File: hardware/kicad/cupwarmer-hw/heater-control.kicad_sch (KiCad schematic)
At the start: 10 parts, among them Q1 AO3400 SOT-23

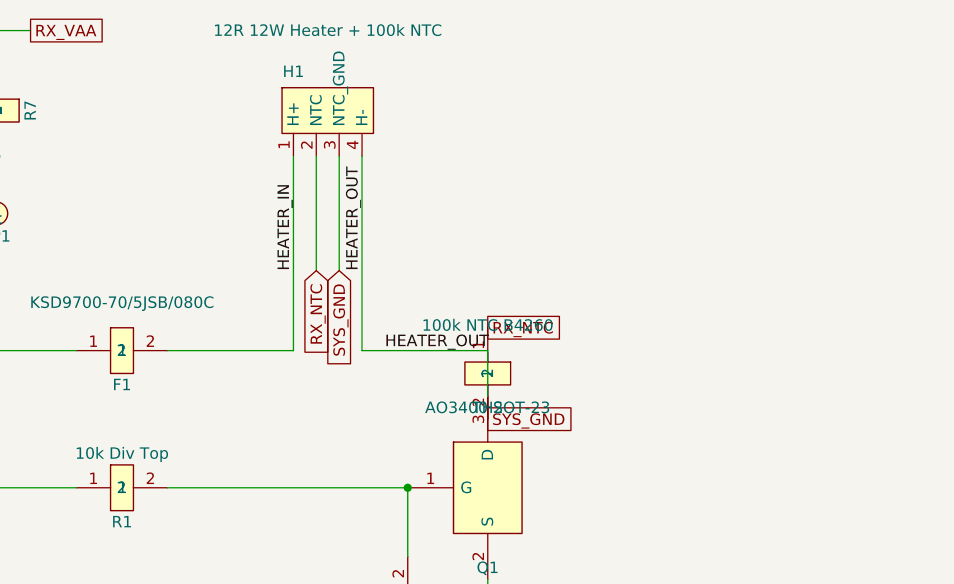
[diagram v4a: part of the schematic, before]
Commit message: Add R_HTR off-board to model heater coil; relabel H1
Pair TH2 with R_HTR (12 ohm, 12 W coil) so the heater assembly's
internals (heater + NTC) are explicit on the schematic but excluded
from the board (on_board=no, empty Footprint). H1's Value drops
the redundant element description and now reads "4-pin heater
harness connector" — H1 is just the connector boundary; the actual
parts live in R_HTR and TH2.

Co-Authored-By: Claude Opus 4.7 (1M context) <noreply@anthropic.com>
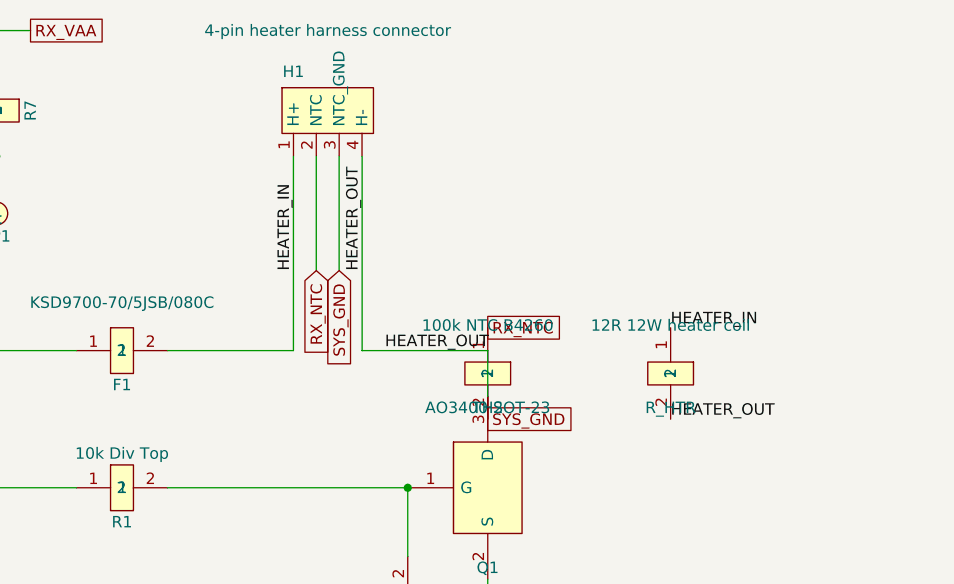
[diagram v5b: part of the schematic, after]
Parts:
- added R_HTR: 12R 12W heater coil, symbol cupwarmer:PASSIVE_2
- H1: value 12R 12W Heater + 100k NTC -> 4-pin heater harness connector
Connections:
- net HEATER_IN: now also R_HTR.1
- net HEATER_OUT: now also R_HTR.2
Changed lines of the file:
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@@
+	)
+	(label "HEATER_OUT"
+		(at 116.84 66.04 0)
+		(effects
+			(font
+				(size 1.27 1.27)
+			)
+			(justify left bottom)
+		)
+	)
+	(label "HEATER_IN"
+		(at 116.84 55.88 0)
+		(effects
+			(font
+				(size 1.27 1.27)
+			)
+			(justify left bottom)
+		)
 	)
 	(label "HEATER_OUT"
@@
 	(symbol
 		(lib_id "cupwarmer:PASSIVE_2")
+		(at 116.84 60.96 270)
+		(unit 1)
+		(body_style 1)
+		(exclude_from_sim no)
+		(in_bom yes)
+		(on_board no)
+		(in_pos_files yes)
+		(dnp no)
+		(property "Reference" "R_HTR"
+			(at 116.84 64.77 270)
+			(show_name no)
+			(do_not_autoplace no)
+			(effects
+				(font
+					(size 1.27 1.27)
+				)
+			)
+		)
+		(property "Value" "12R 12W heater coil"
+			(at 116.84 55.626 270)
+			(show_name no)
+			(do_not_autoplace no)
+			(effects
+				(font
+					(size 1.27 1.27)
+				)
+			)
+		)
+		(property "Footprint" ""
+			(at 116.84 60.96 270)
+			(hide yes)
+			(show_name no)
+			(do_not_autoplace no)
+			(effects
+				(font
+					(size 1.27 1.27)
+				)
+			)
+		)
+		(property "Datasheet" "~"
+			(at 116.84 60.96 270)
+			(hide yes)
+			(show_name no)
+			(do_not_autoplace no)
+			(effects
+				(font
+					(size 1.27 1.27)
+				)
+			)
+		)
+		(property "Description" "Silicone heater element inside H1 harness; 12 ohm, 12 W nominal, off-board"
+			(at 116.84 60.96 270)
+			(hide yes)
+			(show_name no)
+			(do_not_autoplace no)
+			(effects
+				(font
+					(size 1.27 1.27)
+				)
+			)
+		)
+		(property "Manufacturer" ""
+			(at 0 0 0)
+			(hide yes)
+			(show_name no)
+			(do_not_autoplace no)
+			(effects
+				(font
+					(size 1.27 1.27)
+				)
+			)
+		)
+		(property "LCSC" ""
+			(at 0 0 0)
+			(hide yes)
+			(show_name no)
+			(do_not_autoplace no)
+			(effects
+				(font
+					(size 1.27 1.27)
+				)
+			)
+		)
+		(property "MPN" ""
+			(at 0 0 0)
+			(hide yes)
+			(show_name no)
+			(do_not_autoplace no)
+			(effects
+				(font
+					(size 1.27 1.27)
+				)
+			)
+		)
+		(pin "1"
+		)
+		(pin "2"
+		)
+		(instances
+			(project "cupwarmer-hw"
+				(path "/f3c63676-f392-4700-9f58-a6787e1eb284/22222222-2222-2222-2222-222222222222"
+					(reference "R_HTR")
+					(unit 1)
+				)
+			)
+		)
+	)
+	(symbol
+		(lib_id "cupwarmer:PASSIVE_2")
 		(at 96.52 60.96 270)
 		(unit 1)
@@
 			)
 		)
-		(property "Value" "12R 12W Heater + 100k NTC"
+		(property "Value" "4-pin heater harness connector"
 			(at 78.74 22.86 0)
 			(show_name no)

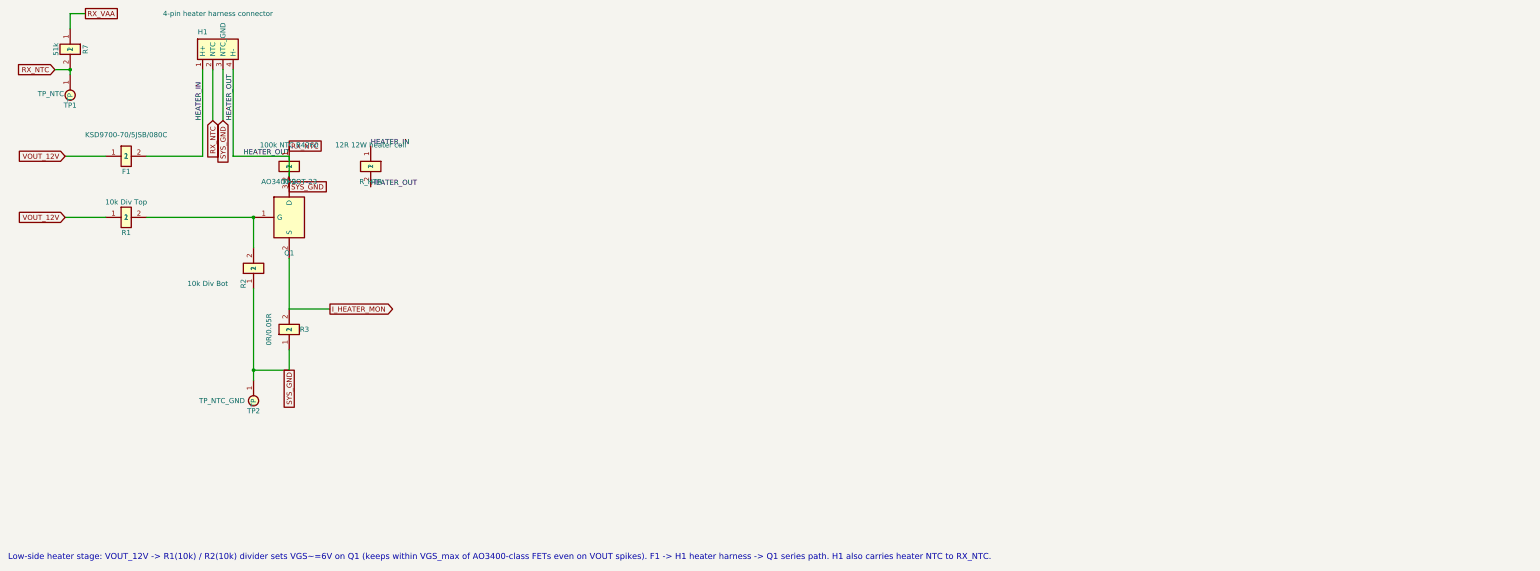
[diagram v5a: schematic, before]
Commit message: Mark H2 off-board; relabel H1/H2 as PCB-side / heater-side
Add H2 as the heater-side 4-pin connector, paired with H1 on the PCB
side. H2/F1/TH2/R_HTR remain visible on the schematic for
documentation of the heater assembly, but are excluded from the PCB
netlist via on_board=no.

Co-Authored-By: Claude Opus 4.7 (1M context) <noreply@anthropic.com>
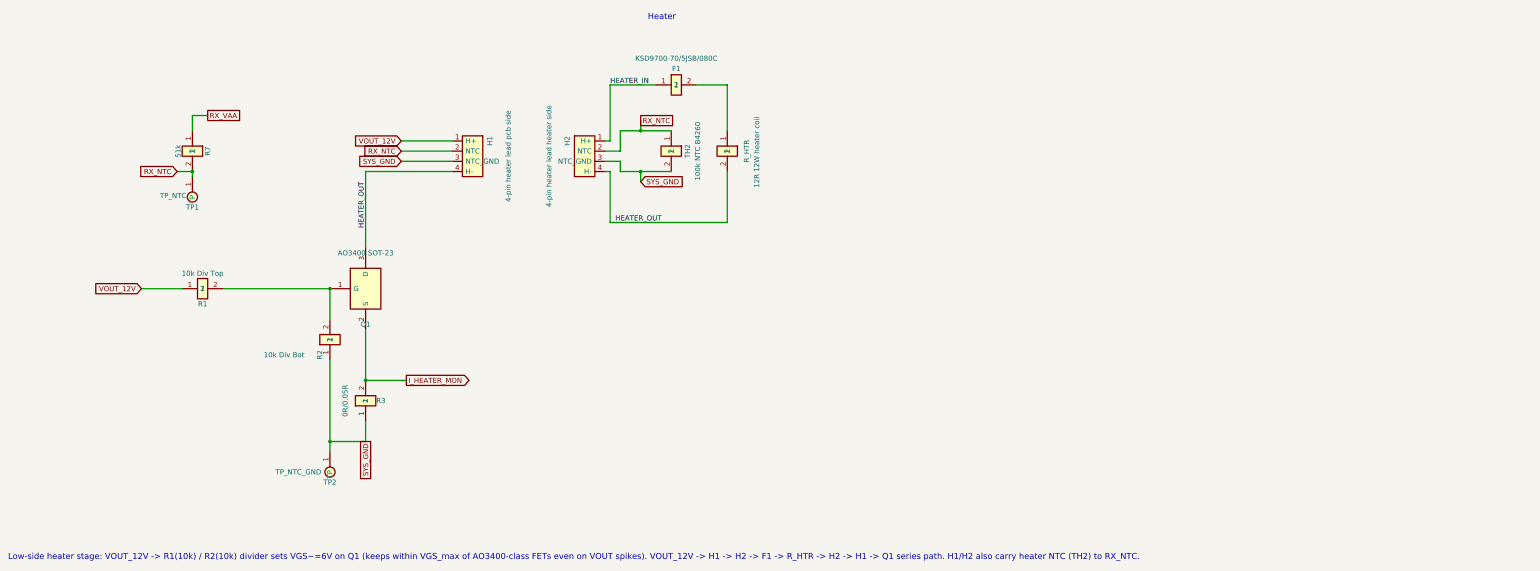
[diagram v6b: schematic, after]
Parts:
- added H2: 4-pin heater lead heater side, cupwarmer:SolderWire-HeaterHarness_1x04_P5.0mm_D1.4mm, symbol cupwarmer:HEATER_HARNESS_4
- H1: value 4-pin heater harness connector -> 4-pin heater lead pcb side
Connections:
- net HEATER_IN: now also F1.1, H2.1 (H+); no longer F1.2, H1.1 (H+), R_HTR.1
- net HEATER_OUT: now also H2.4 (H-)
- net RX_NTC: now also H2.2 (NTC)
- net SYS_GND: now also H2.3 (NTC_GND)
- net VOUT_12V: now also H1.1 (H+); no longer F1.1
- new net: F1.2, R_HTR.1
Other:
- note added: "Heater"
- note added: "Low-side heater stage: VOUT_12V -> R1(10k) / R2(10k) divider sets VGS~=6V on Q1 (keeps within VGS_max of AO3400-class FETs even on VOUT spikes). VOUT_12V -> H1 -> H2 -> F1 -> R_HTR -> H2 -> H1 -> Q1 series path. H1/H2 also carry heater NTC (TH2) to RX_NTC."
- note removed: "Low-side heater stage: VOUT_12V -> R1(10k) / R2(10k) divider sets VGS~=6V on Q1 (keeps within VGS_max of AO3400-class FETs even on VOUT spikes). F1 -> H1 heater harness -> Q1 series path. H1 also carries heater NTC to RX_NTC."
- moved on the sheet: F1, H1, Q1, R1, R2, R3, R7, R_HTR, TH2, TP1, TP2

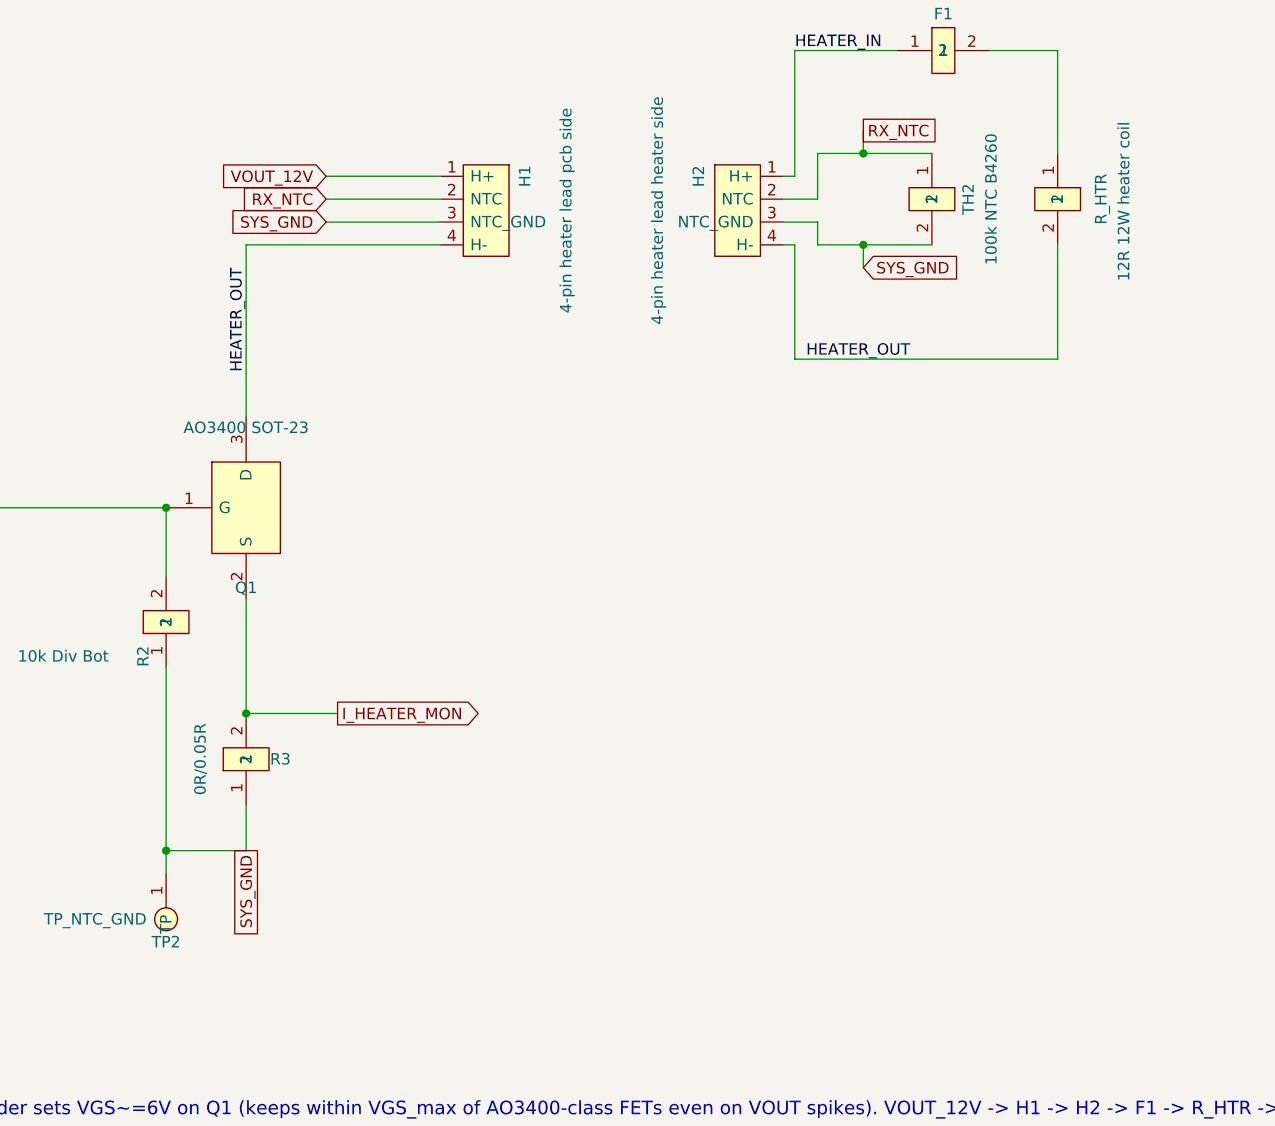
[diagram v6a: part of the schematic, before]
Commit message: Replace J3 bring-up header with TP3 test pad on I_HEATER_MON
Drop the dual-purpose 2-pin J3 (RX_INTB + I_HEATER_MON bring-up) and
expose only I_HEATER_MON via a single-pin TP3 test pad matching
TP1/TP2 (TESTPAD_1 symbol, 1x01 pin header footprint). RX_INTB stays
internal to the U1.H4 ↔ R12.1 path with its label moved onto that
net.

Co-Authored-By: Claude Opus 4.7 (1M context) <noreply@anthropic.com>
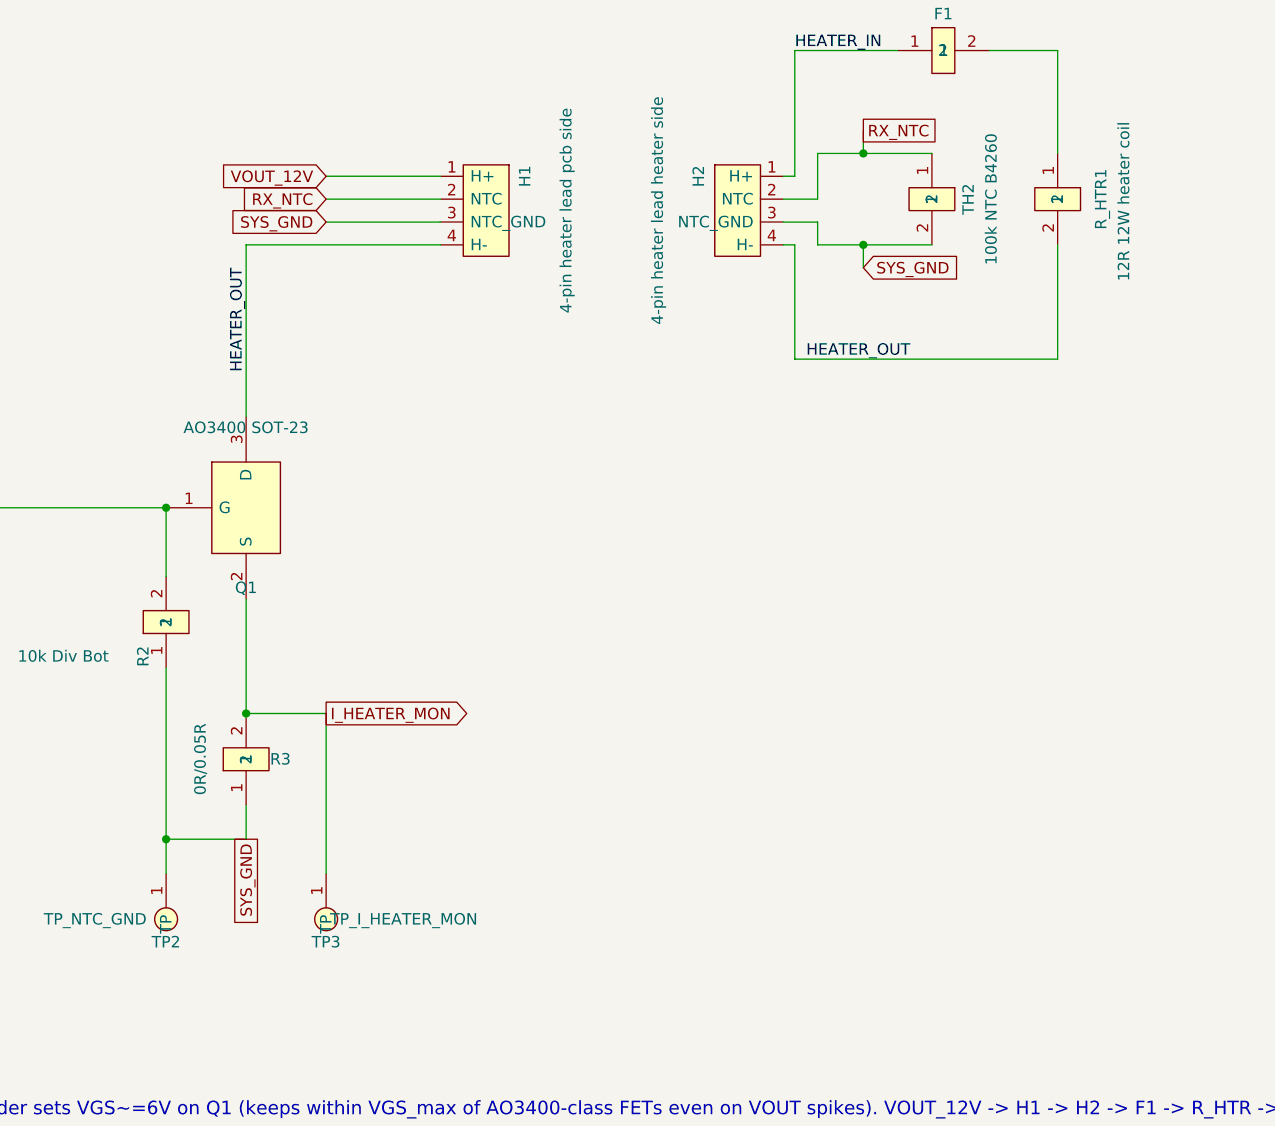
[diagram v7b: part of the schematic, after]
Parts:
- added TP3: TP_I_HEATER_MON, Connector_PinHeader_2.54mm:PinHeader_1x01_P2.54mm_Vertical, symbol cupwarmer:TESTPAD_1
- TP1, TP2: footprint cupwarmer:TestPoint_Pad_D1.0mm_NoSilk -> Connector_PinHeader_2.54mm:PinHeader_1x01_P2.54mm_Vertical
- renumbered R_HTR to R_HTR1
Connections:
- net I_HEATER_MON: now also TP3.1 (TP)
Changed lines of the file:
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@@
+	)
+	(junction
+		(at 106.68 128.27)
+		(diameter 0)
+		(color 0 0 0 0)
 	)
 	(junction
@@
 	)
 	(junction
-		(at 115.57 114.3)
+		(at 72.39 62.23)
 		(diameter 0)
 		(color 0 0 0 0)
 	)
 	(junction
-		(at 106.68 129.54)
-		(diameter 0)
-		(color 0 0 0 0)
-	)
-	(junction
-		(at 72.39 62.23)
+		(at 115.57 114.3)
 		(diameter 0)
 		(color 0 0 0 0)
@@
 	(wire
 		(pts
-			(xy 106.68 132.08) (xy 106.68 129.54)
-		)
-		(stroke
-			(width 0)
-			(type default)
-		)
-	)
-	(wire
-		(pts
 			(xy 115.57 101.6) (xy 115.57 114.3)
 		)
@@
 	(wire
 		(pts
-			(xy 115.57 124.46) (xy 115.57 129.54)
+			(xy 115.57 124.46) (xy 115.57 128.27)
 		)
 		(stroke
@@
 	(wire
 		(pts
-			(xy 115.57 114.3) (xy 125.73 114.3)
+			(xy 115.57 114.3) (xy 124.46 114.3)
 		)
 		(stroke
@@
 	(wire
 		(pts
-			(xy 106.68 109.22) (xy 106.68 129.54)
+			(xy 106.68 109.22) (xy 106.68 128.27)
 		)
 		(stroke
@@
 	(wire
 		(pts
-			(xy 106.68 129.54) (xy 115.57 129.54)
+			(xy 106.68 128.27) (xy 115.57 128.27)
 		)
 		(stroke
@@
 	(wire
 		(pts
+			(xy 124.46 114.3) (xy 124.46 132.08)
+		)
+		(stroke
+			(width 0)
+			(type default)
+		)
+	)
+	(wire
+		(pts
 			(xy 176.53 54.61) (xy 175.26 54.61)
+		)
+		(stroke
+			(width 0)
+			(type default)
+		)
+	)
+	(wire
+		(pts
+			(xy 106.68 128.27) (xy 106.68 132.08)
 		)
 		(stroke
@@
 	(global_label "I_HEATER_MON"
 		(shape output)
-		(at 125.73 114.3 0)
+		(at 124.46 114.3 0)
 		(effects
 			(font
@@
 		)
 		(property "Intersheetrefs" "${INTERSHEET_REFS}"
-			(at 125.73 114.3 0)
+			(at 124.46 114.3 0)
 			(hide yes)
 			(show_name no)
@@
 	(global_label "SYS_GND"
 		(shape passive)
-		(at 115.57 129.54 270)
+		(at 115.57 128.27 270)
 		(effects
 			(font
@@
 		)
 		(property "Intersheetrefs" "${INTERSHEET_REFS}"
-			(at 115.57 129.54 0)
+			(at 115.57 128.27 0)
 			(hide yes)
 			(show_name no)
@@
 				(font
 					(size 1.27 1.27)
+				)
+			)
+		)
+	)
+	(symbol
+		(lib_id "cupwarmer:TESTPAD_1")
+		(at 124.46 137.16 0)
+		(unit 1)
+		(body_style 1)
+		(exclude_from_sim no)
+		(in_bom no)
+		(on_board yes)
+		(in_pos_files no)
+		(dnp no)
+		(property "Reference" "TP3"
+			(at 124.46 139.7 0)
+			(show_name no)
+			(do_not_autoplace no)
+			(effects
+				(font
+					(size 1.27 1.27)
+				)
+			)
+		)
+		(property "Value" "TP_I_HEATER_MON"
+			(at 133.096 137.16 0)
+			(show_name no)
+			(do_not_autoplace no)
+			(effects
+				(font
+					(size 1.27 1.27)
+				)
+			)
+		)
+		(property "Footprint" "Connector_PinHeader_2.54mm:PinHeader_1x01_P2.54mm_Vertical"
+			(at 124.46 137.16 0)
+			(hide yes)
+			(show_name no)
+			(do_not_autoplace no)
+			(effects
+				(font
+					(size 1.27 1.27)
+				)
+			)
+		)
+		(property "Datasheet" "~"
+			(at 124.46 137.16 0)
+			(hide yes)
+			(show_name no)
+			(do_not_autoplace no)
+			(effects
+				(font
+					(size 1.27 1.27)
+				)
+			)
+		)
+		(property "Description" "DMM probe pad for heater current monitor"
+			(at 124.46 137.16 0)
+			(hide yes)
+			(show_name no)
+			(do_not_autoplace no)
+			(effects
+				(font
+					(size 1.27 1.27)
+				)
+			)
+		)
+		(pin "1"
+		)
+		(instances
+			(project "cupwarmer-hw"
+				(path "/f3c63676-f392-4700-9f58-a6787e1eb284/22222222-2222-2222-2222-222222222222"
+					(reference "TP3")
+					(unit 1)
 				)
 			)
@@
 			)
 		)
-		(property "Footprint" "cupwarmer:TestPoint_Pad_D1.0mm_NoSilk"
+		(property "Footprint" "Connector_PinHeader_2.54mm:PinHeader_1x01_P2.54mm_Vertical"
 			(at 72.39 68.58 0)
 			(hide yes)
@@
 			)
 		)
-		(property "Footprint" "cupwarmer:TestPoint_Pad_D1.0mm_NoSilk"
+		(property "Footprint" "Connector_PinHeader_2.54mm:PinHeader_1x01_P2.54mm_Vertical"
 			(at 106.68 137.16 0)
 			(hide yes)
@@
 		(in_pos_files yes)
 		(dnp no)
-		(property "Reference" "R_HTR"
+		(property "Reference" "R_HTR1"
 			(at 210.566 57.15 0)
 			(show_name no)
@@
 			(project "cupwarmer-hw"
 				(path "/f3c63676-f392-4700-9f58-a6787e1eb284/22222222-2222-2222-2222-222222222222"
-					(reference "R_HTR")
+					(reference "R_HTR1")
 					(unit 1)
 				)
